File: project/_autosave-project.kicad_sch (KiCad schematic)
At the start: 0 parts

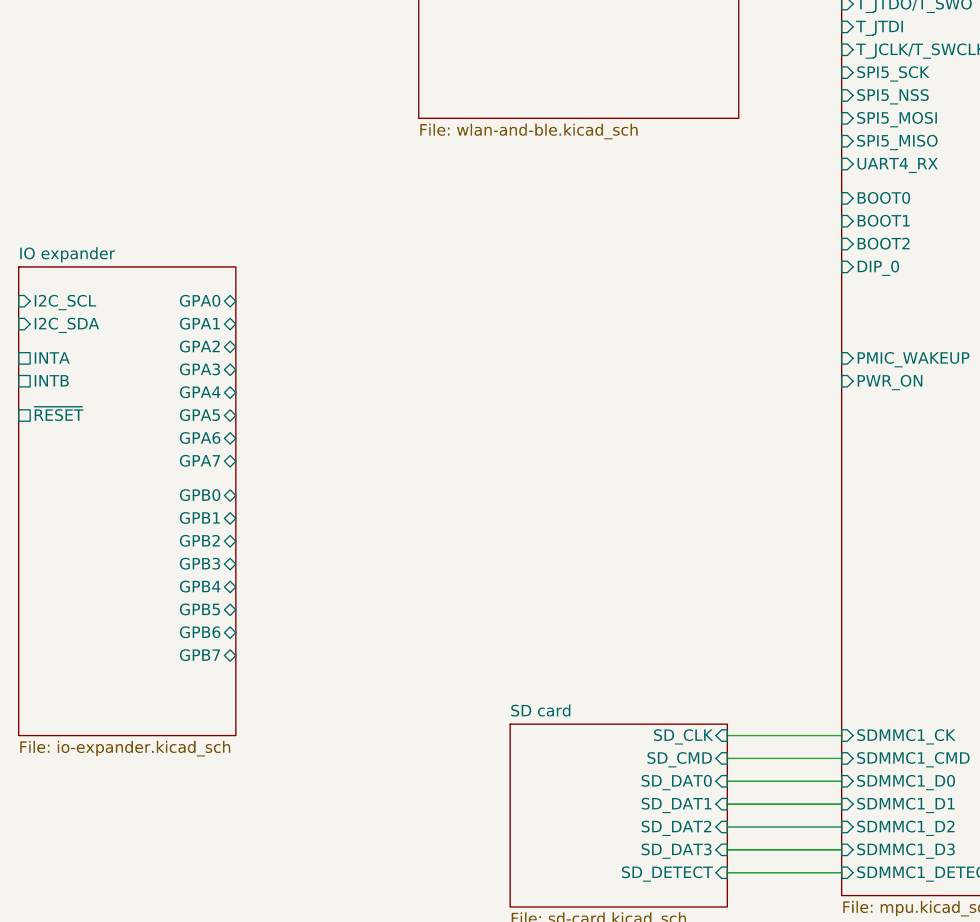
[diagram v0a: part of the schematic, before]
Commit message: Added CubeMX project and some schematic components are added
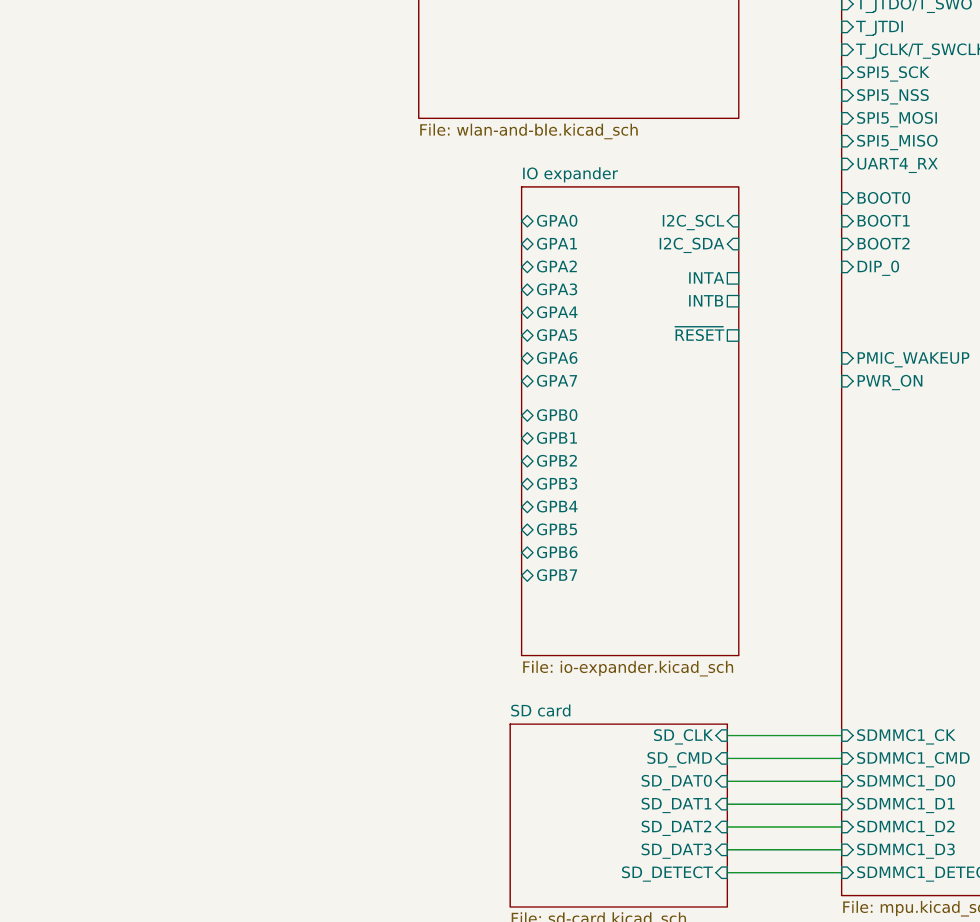
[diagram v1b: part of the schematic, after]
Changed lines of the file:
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@@
 	)
 	(sheet
-		(at 38.1 184.15)
+		(at 93.98 175.26)
 		(size 24.13 52.07)
 		(exclude_from_sim no)
@@
 		)
 		(property "Sheetname" "IO expander"
-			(at 38.1 183.4384 0)
+			(at 93.98 174.5484 0)
 			(effects
 				(font
@@
 		)
 		(property "Sheetfile" "io-expander.kicad_sch"
-			(at 38.1 236.8046 0)
+			(at 93.98 227.9146 0)
 			(effects
 				(font
@@
 		)
 		(pin "GPA0" bidirectional
-			(at 62.23 187.96 0)
-			(effects
-				(font
-					(size 1.27 1.27)
-				)
-				(justify right)
+			(at 93.98 179.07 180)
+			(effects
+				(font
+					(size 1.27 1.27)
+				)
+				(justify left)
 			)
 		)
 		(pin "GPA1" bidirectional
-			(at 62.23 190.5 0)
-			(effects
-				(font
-					(size 1.27 1.27)
-				)
-				(justify right)
+			(at 93.98 181.61 180)
+			(effects
+				(font
+					(size 1.27 1.27)
+				)
+				(justify left)
 			)
 		)
 		(pin "GPA2" bidirectional
-			(at 62.23 193.04 0)
-			(effects
-				(font
-					(size 1.27 1.27)
-				)
-				(justify right)
+			(at 93.98 184.15 180)
+			(effects
+				(font
+					(size 1.27 1.27)
+				)
+				(justify left)
 			)
 		)
 		(pin "GPA3" bidirectional
-			(at 62.23 195.58 0)
-			(effects
-				(font
-					(size 1.27 1.27)
-				)
-				(justify right)
+			(at 93.98 186.69 180)
+			(effects
+				(font
+					(size 1.27 1.27)
+				)
+				(justify left)
 			)
 		)
 		(pin "GPA4" bidirectional
-			(at 62.23 198.12 0)
-			(effects
-				(font
-					(size 1.27 1.27)
-				)
-				(justify right)
+			(at 93.98 189.23 180)
+			(effects
+				(font
+					(size 1.27 1.27)
+				)
+				(justify left)
 			)
 		)
 		(pin "GPA5" bidirectional
-			(at 62.23 200.66 0)
-			(effects
-				(font
-					(size 1.27 1.27)
-				)
-				(justify right)
+			(at 93.98 191.77 180)
+			(effects
+				(font
+					(size 1.27 1.27)
+				)
+				(justify left)
 			)
 		)
 		(pin "GPA6" bidirectional
-			(at 62.23 203.2 0)
-			(effects
-				(font
-					(size 1.27 1.27)
-				)
-				(justify right)
+			(at 93.98 194.31 180)
+			(effects
+				(font
+					(size 1.27 1.27)
+				)
+				(justify left)
 			)
 		)
 		(pin "GPA7" bidirectional
-			(at 62.23 205.74 0)
-			(effects
-				(font
-					(size 1.27 1.27)
-				)
-				(justify right)
+			(at 93.98 196.85 180)
+			(effects
+				(font
+					(size 1.27 1.27)
+				)
+				(justify left)
 			)
 		)
 		(pin "GPB0" bidirectional
-			(at 62.23 209.55 0)
-			(effects
-				(font
-					(size 1.27 1.27)
-				)
-				(justify right)
+			(at 93.98 200.66 180)
+			(effects
+				(font
+					(size 1.27 1.27)
+				)
+				(justify left)
 			)
 		)
 		(pin "GPB1" bidirectional
-			(at 62.23 212.09 0)
-			(effects
-				(font
-					(size 1.27 1.27)
-				)
-				(justify right)
+			(at 93.98 203.2 180)
+			(effects
+				(font
+					(size 1.27 1.27)
+				)
+				(justify left)
 			)
 		)
 		(pin "GPB2" bidirectional
-			(at 62.23 214.63 0)
-			(effects
-				(font
-					(size 1.27 1.27)
-				)
-				(justify right)
+			(at 93.98 205.74 180)
+			(effects
+				(font
+					(size 1.27 1.27)
+				)
+				(justify left)
 			)
 		)
 		(pin "GPB3" bidirectional
-			(at 62.23 217.17 0)
-			(effects
-				(font
-					(size 1.27 1.27)
-				)
-				(justify right)
+			(at 93.98 208.28 180)
+			(effects
+				(font
+					(size 1.27 1.27)
+				)
+				(justify left)
 			)
 		)
 		(pin "GPB4" bidirectional
-			(at 62.23 219.71 0)
-			(effects
-				(font
-					(size 1.27 1.27)
-				)
-				(justify right)
+			(at 93.98 210.82 180)
+			(effects
+				(font
+					(size 1.27 1.27)
+				)
+				(justify left)
 			)
 		)
 		(pin "GPB5" bidirectional
-			(at 62.23 222.25 0)
-			(effects
-				(font
-					(size 1.27 1.27)
-				)
-				(justify right)
+			(at 93.98 213.36 180)
+			(effects
+				(font
+					(size 1.27 1.27)
+				)
+				(justify left)
 			)
 		)
 		(pin "GPB6" bidirectional
-			(at 62.23 224.79 0)
-			(effects
-				(font
-					(size 1.27 1.27)
-				)
-				(justify right)
+			(at 93.98 215.9 180)
+			(effects
+				(font
+					(size 1.27 1.27)
+				)
+				(justify left)
 			)
 		)
 		(pin "GPB7" bidirectional
-			(at 62.23 227.33 0)
-			(effects
-				(font
-					(size 1.27 1.27)
-				)
-				(justify right)
+			(at 93.98 218.44 180)
+			(effects
+				(font
+					(size 1.27 1.27)
+				)
+				(justify left)
 			)
 		)
 		(pin "I2C_SCL" input
-			(at 38.1 187.96 180)
-			(effects
-				(font
-					(size 1.27 1.27)
-				)
-				(justify left)
+			(at 118.11 179.07 0)
+			(effects
+				(font
+					(size 1.27 1.27)
+				)
+				(justify right)
 			)
 		)
 		(pin "I2C_SDA" input
-			(at 38.1 190.5 180)
-			(effects
-				(font
-					(size 1.27 1.27)
-				)
-				(justify left)
+			(at 118.11 181.61 0)
+			(effects
+				(font
+					(size 1.27 1.27)
+				)
+				(justify right)
 			)
 		)
 		(pin "INTA" passive
-			(at 38.1 194.31 180)
-			(effects
-				(font
-					(size 1.27 1.27)
-				)
-				(justify left)
+			(at 118.11 185.42 0)
+			(effects
+				(font
+					(size 1.27 1.27)
+				)
+				(justify right)
 			)
 		)
 		(pin "INTB" passive
-			(at 38.1 196.85 180)
-			(effects
-				(font
-					(size 1.27 1.27)
-				)
-				(justify left)
+			(at 118.11 187.96 0)
+			(effects
+				(font
+					(size 1.27 1.27)
+				)
+				(justify right)
 			)
 		)
 		(pin "~{RESET}" passive
-			(at 38.1 200.66 180)
-			(effects
-				(font
-					(size 1.27 1.27)
-				)
-				(justify left)
-			)
-		)
+			(at 118.11 191.77 0)
+			(effects
+				(font
+					(size 1.27 1.27)
+				)
+				(justify right)
+			)
+		)
